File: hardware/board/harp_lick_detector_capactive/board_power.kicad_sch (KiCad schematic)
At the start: 24 parts, among them J5 Barrel_Jack_Switch, U5 LT3030, U6 LM27762

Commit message: update footprints; populate bom
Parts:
- removed C2, C3: 10nF, Capacitor_SMD:C_0603_1608Metric_Pad1.08x0.95mm_HandSolder, symbol Device:C
- removed R51, R61: 100K, Resistor_SMD:R_0603_1608Metric_Pad0.98x0.95mm_HandSolder, symbol Device:R
- added C32 (x2): 10nF, Capacitor_SMD:C_0402_1005Metric, symbol Device:C
- added R20 (x2): 100K, Resistor_SMD:R_0402_1005Metric, symbol Device:R
- R52: footprint Resistor_SMD:R_0603_1608Metric_Pad0.98x0.95mm_HandSolder -> Resistor_SMD:R_0402_1005Metric; Link https://www.digikey.com/en/products/detail/yageo/RC0603FR-0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 -> https://www.digikey.com/en/products/detail/te-connectivity-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; Manufacturer Yageo -> TE Connectivity Passive Product; Manufacturer Number RC0603FR-07309KL -> CPF0402B309KE1; Notes (none) -> 1% tolerance also OK; Tolerance 1% -> 0.1%
- R62: footprint Resistor_SMD:R_0603_1608Metric_Pad0.98x0.95mm_HandSolder -> Resistor_SMD:R_0402_1005Metric; Link https://www.digikey.com/en/products/detail/stackpole-electr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 -> https://www.digikey.com/en/products/detail/koa-speer-electr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; Manufacturer Stackpole Electronics Inc. -> Koa Speer Electronics, Inc.; Manufacturer Number RNCF0603BKE172K -> RN73H1ETTP1723F25; Tolerance 0.1% -> 1%; Vendor Reel Link (none) -> 2019-RN73H1ETTP1723F25DKR-ND
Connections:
- net +3V3: now also C32.1
- net +5V: now also C32.1
- net GND: now also R20.1, R20.1
- net at R62.2, U5.10 (ADJ2): now also R20.2
- net at U5.9 (BYP2): now also C32.2
- net at R52.2, U5.1 (ADJ1): now also R20.2
- net at U5.2 (BYP1): now also C32.2
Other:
- note added: "TODO: consider polyfuse"
- company: (none) -> The Allen Institute for Neural Dynamics
- title: (none) -> Lickety Split Capacitive Lick Detector

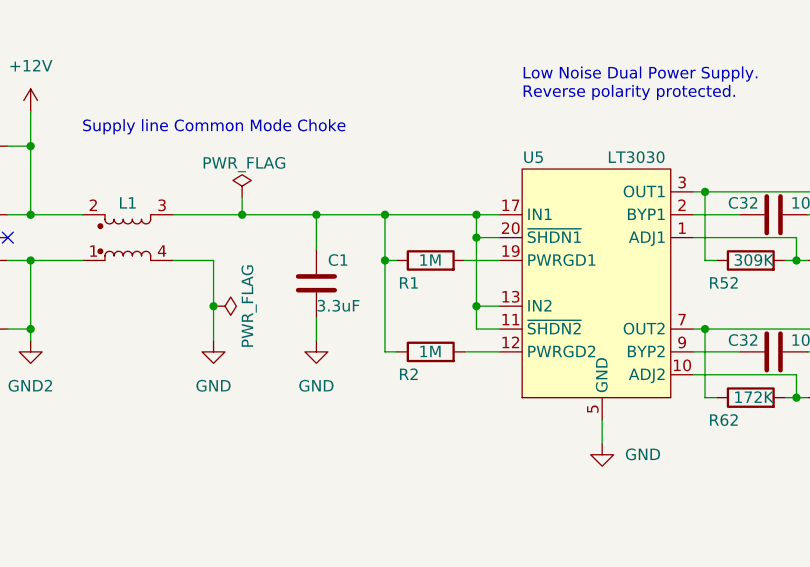
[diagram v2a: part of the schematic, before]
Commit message: update ads7049 pinout
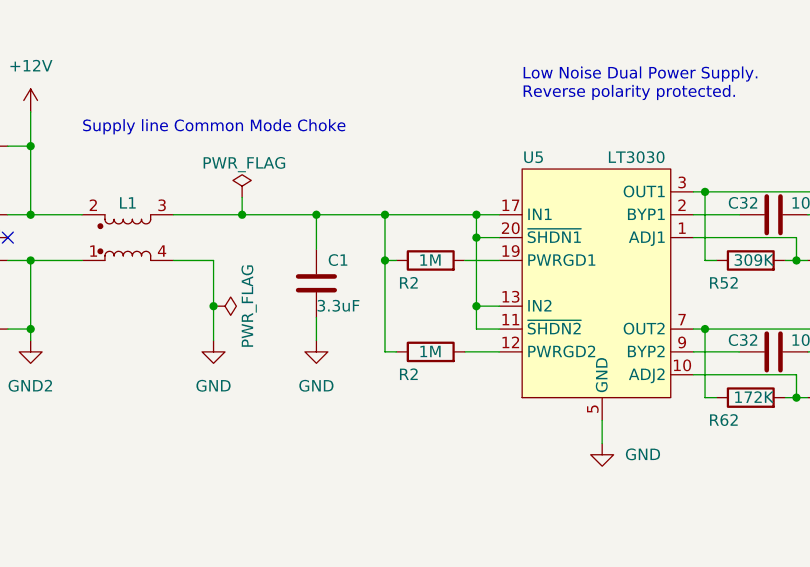
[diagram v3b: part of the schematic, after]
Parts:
- removed R1: 1M, Resistor_SMD:R_0603_1608Metric_Pad0.98x0.95mm_HandSolder, symbol Device:R
- added R2: 1M, Resistor_SMD:R_0402_1005Metric, symbol Device:R
- J5: Manufacturer (none) -> CUI Devices; Manufacturer Number CUI Devices -> PJ-102AH
- R2: footprint Resistor_SMD:R_0603_1608Metric_Pad0.98x0.95mm_HandSolder -> Resistor_SMD:R_0402_1005Metric; Link https://www.digikey.com/en/products/detail/te-connectivity-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 -> https://www.digikey.com/en/products/detail/yageo/RC0402FR-1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; Manufacturer TE Connectivity Passive Product -> Yageo; Manufacturer Number CRGP0603F1M0 -> RC0402FR-101ML; PCBWay Link https://www.pcbway.com/components/detail/CRGP0603F1M0/44302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 -> https://www.pcbway.com/components/detail/RC0402FR101ML/1269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
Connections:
- net IN1: now also R2.1
- net at U5.19 (PWRGD1): now also R2.2
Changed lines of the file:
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@@
+    )
+  )
+  (symbol (lib_id "Device:R") (at 114.3 57.15 90) (unit 1)
+    (in_bom yes) (on_board yes) (dnp no)
+    (property "Reference" "R2" (at 113.03 59.69 90)
+      (effects (font (size 1.27 1.27)) (justify left))
+    )
+    (property "Value" "1M" (at 115.57 57.15 90)
+      (effects (font (size 1.27 1.27)) (justify left))
+    )
+    (property "Footprint" "Resistor_SMD:R_0402_1005Metric" (at 114.3 58.928 90)
+      (effects (font (size 1.27 1.27)) hide)
+    )
+    (property "Datasheet" "https://www.yageo.com/upload/media/product/productsearch/datasheet/rchip/PYu-RC_Group_51_RoHS_L_12.pdf" (at 114.3 57.15 0)
+      (effects (font (size 1.27 1.27)) hide)
+    )
+    (property "Link" "https://www.digikey.com/en/products/detail/yageo/RC0402FR-101ML/16982190" (at 114.3 57.15 0)
+      (effects (font (size 1.27 1.27)) hide)
+    )
+    (property "Manufacturer" "Yageo" (at 114.3 57.15 0)
+      (effects (font (size 1.27 1.27)) hide)
+    )
+    (property "Manufacturer Number" "RC0402FR-101ML" (at 114.3 57.15 0)
+      (effects (font (size 1.27 1.27)) hide)
+    )
+    (property "Tolerance" "1%" (at 114.3 57.15 0)
+      (effects (font (size 1.27 1.27)) hide)
+    )
+    (property "PCBWay Link" "https://www.pcbway.com/components/detail/RC0402FR101ML/1269302/" (at 114.3 57.15 0)
+      (effects (font (size 1.27 1.27)) hide)
+    )
+    (pin "1")
+    (pin "2")
+    (instances
+      (project "harp_lick_detector_capactive"
+        (path "/e63e39d7-6ac0-4ffd-8aa3-1841a4541b55"
+          (reference "R2") (unit 1)
+        )
+        (path "/e63e39d7-6ac0-4ffd-8aa3-1841a4541b55/b51b21ef-b374-4f9f-a058-7db9b64fdf4a"
+          (reference "R36") (unit 1)
+        )
+      )
     )
   )
@@
       (effects (font (size 1.27 1.27)) (justify left))
     )
-    (property "Footprint" "Resistor_SMD:R_0603_1608Metric_Pad0.98x0.95mm_HandSolder" (at 114.3 69.088 90)
-      (effects (font (size 1.27 1.27)) hide)
-    )
-    (property "Datasheet" "https://www.te.com/usa-en/product-6-2176326-1.datasheet.pdf" (at 114.3 67.31 0)
-      (effects (font (size 1.27 1.27)) hide)
-    )
-    (property "Link" "https://www.digikey.com/en/products/detail/te-connectivity-passive-product/CRGP0603F1M0/8577054" (at 114.3 67.31 0)
-      (effects (font (size 1.27 1.27)) hide)
-    )
-    (property "Manufacturer" "TE Connectivity Passive Product" (at 114.3 67.31 0)
-      (effects (font (size 1.27 1.27)) hide)
-    )
-    (property "Manufacturer Number" "CRGP0603F1M0" (at 114.3 67.31 0)
+    (property "Footprint" "Resistor_SMD:R_0402_1005Metric" (at 114.3 69.088 90)
+      (effects (font (size 1.27 1.27)) hide)
+    )
+    (property "Datasheet" "https://www.yageo.com/upload/media/product/productsearch/datasheet/rchip/PYu-RC_Group_51_RoHS_L_12.pdf" (at 114.3 67.31 0)
+      (effects (font (size 1.27 1.27)) hide)
+    )
+    (property "Link" "https://www.digikey.com/en/products/detail/yageo/RC0402FR-101ML/16982190" (at 114.3 67.31 0)
+      (effects (font (size 1.27 1.27)) hide)
+    )
+    (property "Manufacturer" "Yageo" (at 114.3 67.31 0)
+      (effects (font (size 1.27 1.27)) hide)
+    )
+    (property "Manufacturer Number" "RC0402FR-101ML" (at 114.3 67.31 0)
       (effects (font (size 1.27 1.27)) hide)
     )
@@
       (effects (font (size 1.27 1.27)) hide)
     )
-    (property "PCBWay Link" "https://www.pcbway.com/components/detail/CRGP0603F1M0/443023/" (at 114.3 67.31 0)
+    (property "PCBWay Link" "https://www.pcbway.com/components/detail/RC0402FR101ML/1269302/" (at 114.3 67.31 0)
       (effects (font (size 1.27 1.27)) hide)
     )
@@
         (path "/e63e39d7-6ac0-4ffd-8aa3-1841a4541b55/b51b21ef-b374-4f9f-a058-7db9b64fdf4a"
           (reference "L1") (unit 1)
-        )
-      )
-    )
-  )
-  (symbol (lib_id "Device:R") (at 114.3 57.15 90) (unit 1)
-    (in_bom yes) (on_board yes) (dnp no)
-    (property "Reference" "R1" (at 113.03 59.69 90)
-      (effects (font (size 1.27 1.27)) (justify left))
-    )
-    (property "Value" "1M" (at 115.57 57.15 90)
-      (effects (font (size 1.27 1.27)) (justify left))
-    )
-    (property "Footprint" "Resistor_SMD:R_0603_1608Metric_Pad0.98x0.95mm_HandSolder" (at 114.3 58.928 90)
-      (effects (font (size 1.27 1.27)) hide)
-    )
-    (property "Datasheet" "https://www.te.com/usa-en/product-6-2176326-1.datasheet.pdf" (at 114.3 57.15 0)
-      (effects (font (size 1.27 1.27)) hide)
-    )
-    (property "Link" "https://www.digikey.com/en/products/detail/te-connectivity-passive-product/CRGP0603F1M0/8577054" (at 114.3 57.15 0)
-      (effects (font (size 1.27 1.27)) hide)
-    )
-    (property "Manufacturer" "TE Connectivity Passive Product" (at 114.3 57.15 0)
-      (effects (font (size 1.27 1.27)) hide)
-    )
-    (property "Manufacturer Number" "CRGP0603F1M0" (at 114.3 57.15 0)
-      (effects (font (size 1.27 1.27)) hide)
-    )
-    (property "Tolerance" "1%" (at 114.3 57.15 0)
-      (effects (font (size 1.27 1.27)) hide)
-    )
-    (property "PCBWay Link" "https://www.pcbway.com/components/detail/CRGP0603F1M0/443023/" (at 114.3 57.15 0)
-      (effects (font (size 1.27 1.27)) hide)
-    )
-    (pin "1")
-    (pin "2")
-    (instances
-      (project "harp_lick_detector_capactive"
-        (path "/e63e39d7-6ac0-4ffd-8aa3-1841a4541b55"
-          (reference "R1") (unit 1)
-        )
-        (path "/e63e39d7-6ac0-4ffd-8aa3-1841a4541b55/b51b21ef-b374-4f9f-a058-7db9b64fdf4a"
-          (reference "R36") (unit 1)
         )
       )
@@
       (effects (font (size 1.27 1.27)) hide)
     )
-    (property "Manufacturer Number" "CUI Devices" (at 59.69 54.61 0)
+    (property "Manufacturer Number" "PJ-102AH" (at 59.69 54.61 0)
       (effects (font (size 1.27 1.27)) hide)
     )
@@
       (effects (font (size 1.27 1.27)) hide)
     )
+    (property "Manufacturer" "CUI Devices" (at 59.69 54.61 0)
+      (effects (font (size 1.27 1.27)) hide)
+    )

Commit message: draft v0.6.0 board
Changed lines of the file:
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@@
     (title "Lickety Split Capacitive Lick Detector")
     (date "2023-09-01")
-    (rev "0.5")
+    (rev "0.6")
     (company "The Allen Institute for Neural Dynamics")
   )
@@
   (junction (at 109.22 57.15) (diameter 0) (color 0 0 0 0)
   )
-  (junction (at 177.165 64.77) (diameter 0) (color 0 0 0 0)
-  )
   (junction (at 119.38 62.23) (diameter 0) (color 0 0 0 0)
   )
@@
   )
   (junction (at 132.08 141.605) (diameter 0) (color 0 0 0 0)
-  )
-  (junction (at 214.63 49.53) (diameter 0) (color 0 0 0 0)
   )
   (junction (at 119.38 54.61) (diameter 0) (color 0 0 0 0)
@@
     (stroke (width 0) (type default))
   )
-  (wire (pts (xy 214.63 49.53) (xy 223.52 49.53))
-    (stroke (width 0) (type default))
-  )
   (wire (pts (xy 185.42 127.635) (xy 184.15 127.635))
     (stroke (width 0) (type default))
@@
     (stroke (width 0) (type default))
   )
-  (wire (pts (xy 177.165 64.77) (xy 160.02 64.77))
+  (wire (pts (xy 160.02 64.77) (xy 186.055 64.77))
     (stroke (width 0) (type default))
   )
@@
     (stroke (width 0) (type default))
   )
-  (wire (pts (xy 160.02 49.53) (xy 214.63 49.53))
+  (wire (pts (xy 160.02 49.53) (xy 223.52 49.53))
     (stroke (width 0) (type default))
   )
@@
   )
   (wire (pts (xy 120.65 137.795) (xy 115.57 137.795))
-    (stroke (width 0) (type default))
-  )
-  (wire (pts (xy 177.165 64.77) (xy 186.055 64.77))
     (stroke (width 0) (type default))
   )
@@
         (path "/e63e39d7-6ac0-4ffd-8aa3-1841a4541b55/b51b21ef-b374-4f9f-a058-7db9b64fdf4a"
           (reference "#PWR0107") (unit 1)
-        )
-      )
-    )
-  )
-  (symbol (lib_id "power:PWR_FLAG") (at 177.165 64.77 0) (unit 1)
-    (in_bom yes) (on_board yes) (dnp no)
-    (property "Reference" "#FLG03" (at 177.165 62.865 0)
-      (effects (font (size 1.27 1.27)) hide)
-    )
-    (property "Value" "PWR_FLAG" (at 172.72 60.96 0)
-      (effects (font (size 1.27 1.27)) (justify left))
-    )
-    (property "Footprint" "" (at 177.165 64.77 0)
-      (effects (font (size 1.27 1.27)) hide)
-    )
-    (property "Datasheet" "~" (at 177.165 64.77 0)
-      (effects (font (size 1.27 1.27)) hide)
-    )
-    (pin "1")
-    (instances
-      (project "sniff_detector"
-        (path "/084b112d-dcfd-4801-aa54-60bf427059e5"
-          (reference "#FLG03") (unit 1)
-        )
-      )
-      (project "harp_lick_detector_capactive"
-        (path "/e63e39d7-6ac0-4ffd-8aa3-1841a4541b55"
-          (reference "#FLG01") (unit 1)
-        )
-        (path "/e63e39d7-6ac0-4ffd-8aa3-1841a4541b55/b51b21ef-b374-4f9f-a058-7db9b64fdf4a"
-          (reference "#FLG010") (unit 1)
         )
       )
@@
         )
       )
-    )
-  )
-  (symbol (lib_id "power:PWR_FLAG") (at 214.63 49.53 0) (unit 1)
-    (in_bom yes) (on_board yes) (dnp no)
-    (property "Reference" "#FLG03" (at 214.63 47.625 0)
-      (effects (font (size 1.27 1.27)) hide)
-    )
-    (property "Value" "PWR_FLAG" (at 210.185 45.72 0)
-      (effects (font (size 1.27 1.27)) (justify left))
-    )
-    (property "Footprint" "" (at 214.63 49.53 0)
-      (effects (font (size 1.27 1.27)) hide)
-    )
-    (property "Datasheet" "~" (at 214.63 49.53 0)
-      (effects (font (size 1.27 1.27)) hide)
-    )
-    (pin "1")
-    (instances
-      (project "sniff_detector"
-        (path "/084b112d-dcfd-4801-aa54-60bf427059e5"
-          (reference "#FLG03") (unit 1)
-        )
-      )
-      (project "harp_lick_detector_capactive"
-        (path "/e63e39d7-6ac0-4ffd-8aa3-1841a4541b55"
-          (reference "#FLG01") (unit 1)
-        )
-        (path "/e63e39d7-6ac0-4ffd-8aa3-1841a4541b55/b51b21ef-b374-4f9f-a058-7db9b64fdf4a"
-          (reference "#FLG05") (unit 1)
-        )
-      )

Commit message: make r0.6 board snapshot
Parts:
- C4: Alternate (none) -> CL21B106KOQNNNE
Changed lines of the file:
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@@
+      (effects (font (size 1.27 1.27)) hide)
+    )
+    (property "Alternate" "CL21B106KOQNNNE" (at 186.055 71.12 0)
       (effects (font (size 1.27 1.27)) hide)
     )

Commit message: draft v0.7 pcb schematic and layout
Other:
- note removed: "TODO: consider polyfuse"
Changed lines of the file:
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@@
     (effects (font (size 1.27 1.27)) (justify left bottom))
-  )
-  (text "TODO: consider polyfuse" (at 20.32 27.305 0)
-    (effects (font (size 2 2) (thickness 0.4) bold) (justify left bottom))
   )
   (text "VOUT- = -1.22 × (R13 + R14) / R14" (at 158.75 146.685 0)

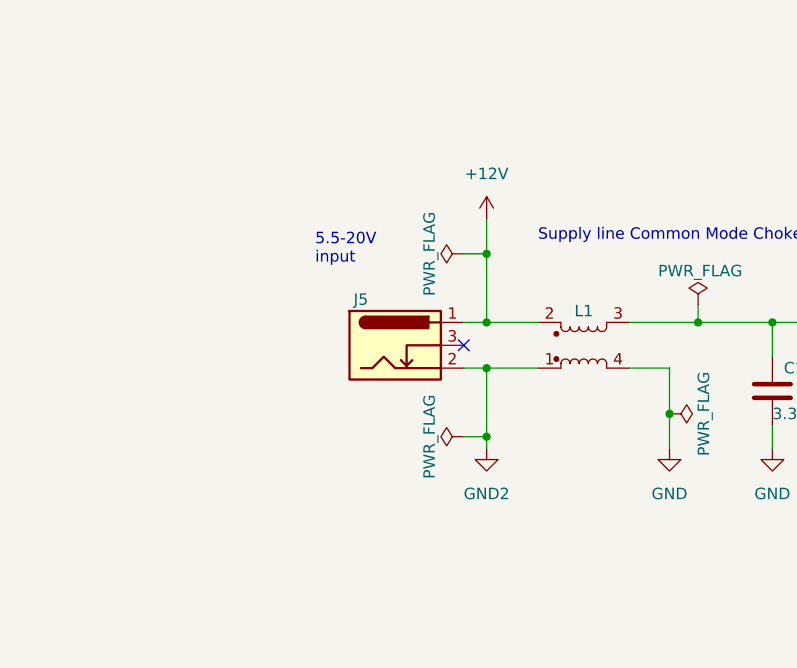
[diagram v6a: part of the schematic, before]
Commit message: implement soe feedback in layout
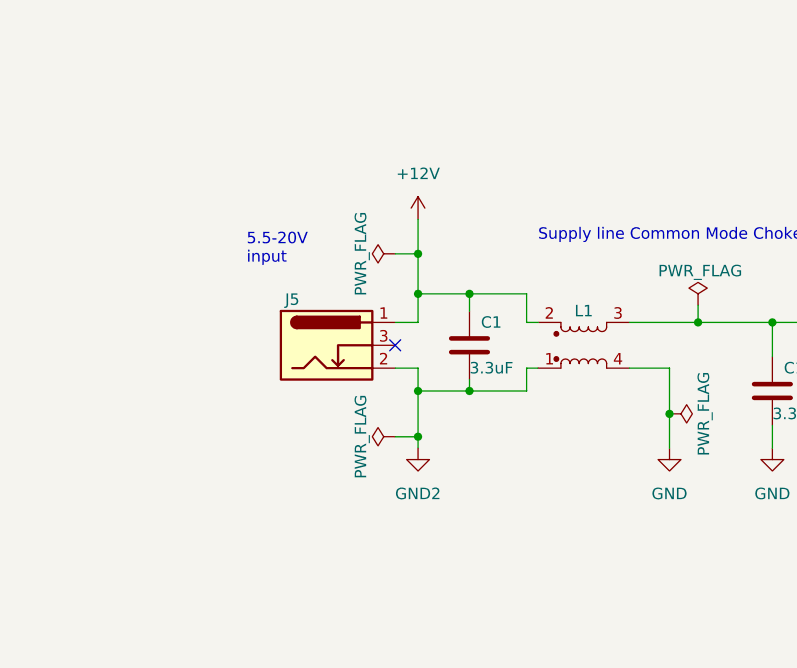
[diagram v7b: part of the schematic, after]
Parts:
- added C1: 3.3uF, Capacitor_SMD:C_0805_2012Metric, symbol Device:C
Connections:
- net +12V: now also C1.1
- net GND2: now also C1.2
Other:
- moved on the sheet: J5

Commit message: draft v0.8 pcb layout
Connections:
- net +3V3 renamed +3.3V
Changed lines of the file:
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@@
       (effects (font (size 1.27 1.27)) hide)
     )
-    (property "Value" "GND" (at 167.64 73.66 90)
+    (property "Value" "GND" (at 165.735 74.93 90)
       (effects (font (size 1.27 1.27)) (justify right))
     )
@@
       (effects (font (size 1.27 1.27)) hide)
     )
-    (property "Value" "GND" (at 167.64 58.42 90)
+    (property "Value" "GND" (at 165.735 59.69 90)
       (effects (font (size 1.27 1.27)) (justify right))
     )
